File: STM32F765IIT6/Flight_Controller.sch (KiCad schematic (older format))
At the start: 1 part

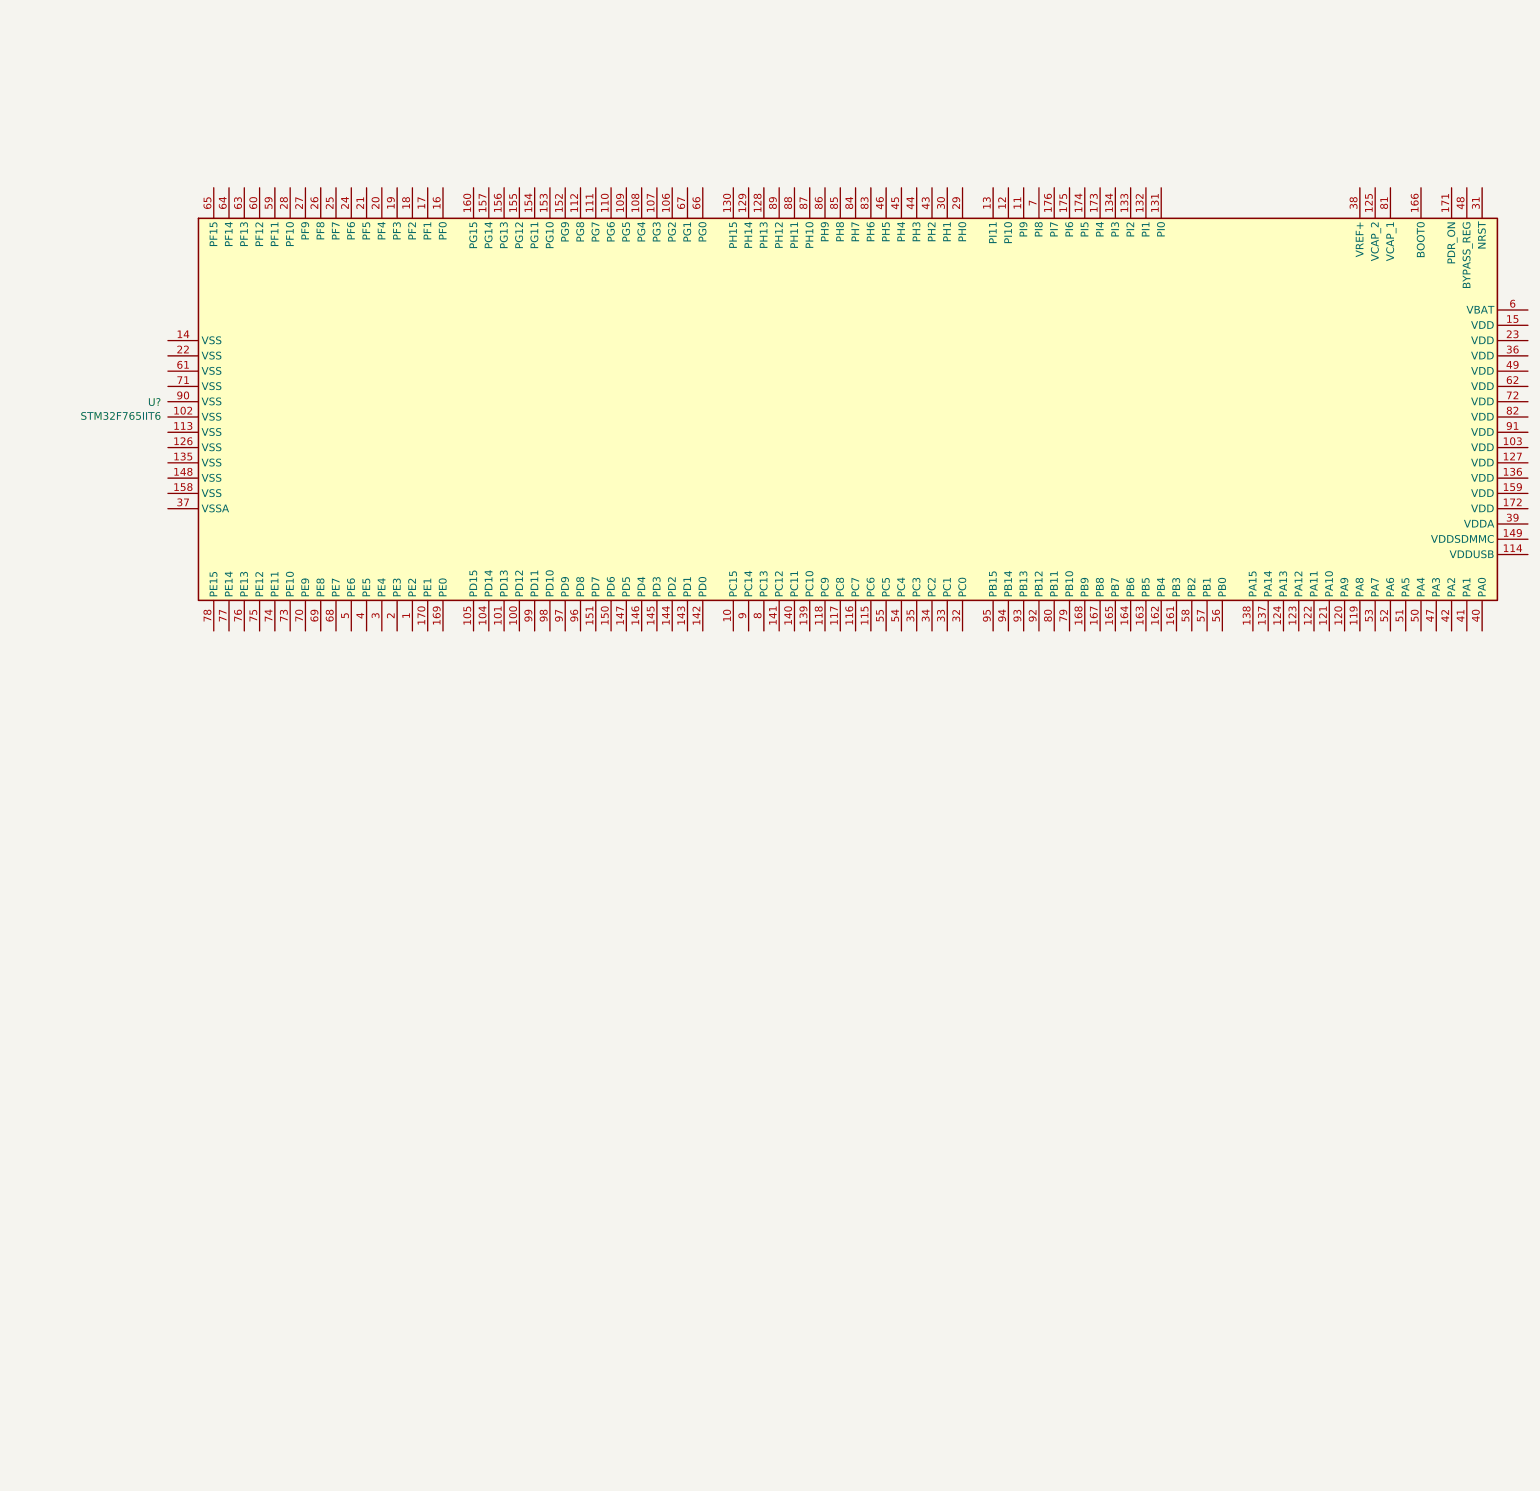
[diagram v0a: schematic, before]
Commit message: Update schematic to include all labels
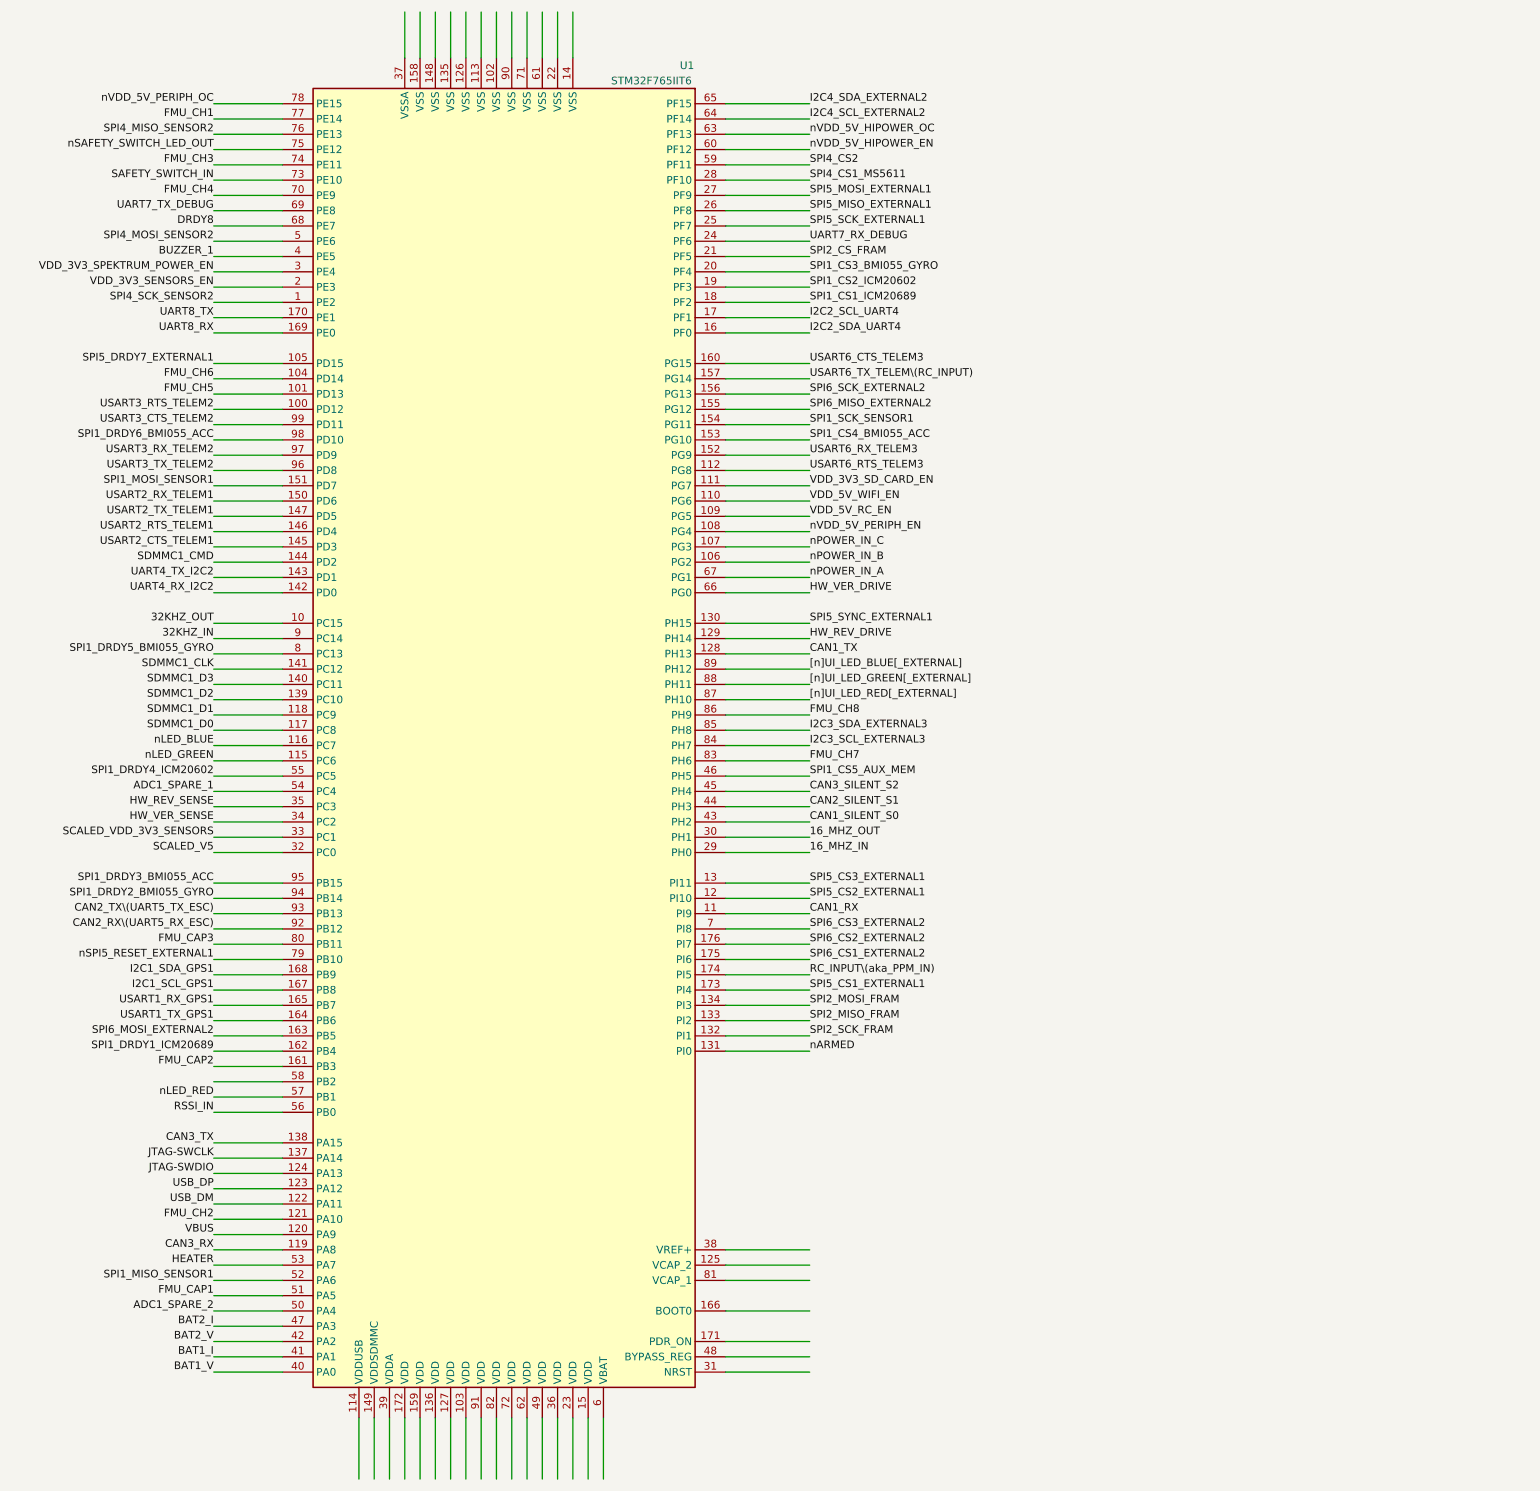
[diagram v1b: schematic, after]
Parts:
- gave numbers to parts that had none: 1
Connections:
- net labels added: 16_MHZ_IN, 16_MHZ_OUT, 32KHZ_IN, 32KHZ_OUT, ADC1_SPARE_1, ADC1_SPARE_2, BAT1_I, BAT1_V, BAT2_I, BAT2_V, BUZZER_1, CAN1_RX, CAN1_SILENT_S0, CAN1_TX, CAN2_RX\(UART5_RX_ESC), CAN2_SILENT_S1, CAN2_TX\(UART5_TX_ESC), CAN3_RX, CAN3_SILENT_S2, CAN3_TX, DRDY8, FMU_CAP1, FMU_CAP2, FMU_CAP3, FMU_CH1, FMU_CH2, FMU_CH3, FMU_CH4, FMU_CH5, FMU_CH6, FMU_CH7, FMU_CH8, HEATER, HW_REV_DRIVE, HW_REV_SENSE, HW_VER_DRIVE, HW_VER_SENSE, I2C1_SCL_GPS1, I2C1_SDA_GPS1, I2C2_SCL_UART4, I2C2_SDA_UART4, I2C3_SCL_EXTERNAL3, I2C3_SDA_EXTERNAL3, I2C4_SCL_EXTERNAL2, I2C4_SDA_EXTERNAL2, JTAG-SWCLK, JTAG-SWDIO, RC_INPUT\(aka_PPM_IN), RSSI_IN, SAFETY_SWITCH_IN, SCALED_V5, SCALED_VDD_3V3_SENSORS, SDMMC1_CLK, SDMMC1_CMD, SDMMC1_D0, SDMMC1_D1, SDMMC1_D2, SDMMC1_D3, SPI1_CS1_ICM20689, SPI1_CS2_ICM20602, SPI1_CS3_BMI055_GYRO, SPI1_CS4_BMI055_ACC, SPI1_CS5_AUX_MEM, SPI1_DRDY1_ICM20689, SPI1_DRDY2_BMI055_GYRO, SPI1_DRDY3_BMI055_ACC, SPI1_DRDY4_ICM20602, SPI1_DRDY5_BMI055_GYRO, SPI1_DRDY6_BMI055_ACC, SPI1_MISO_SENSOR1, SPI1_MOSI_SENSOR1, SPI1_SCK_SENSOR1, SPI2_CS_FRAM, SPI2_MISO_FRAM, SPI2_MOSI_FRAM, SPI2_SCK_FRAM, SPI4_CS1_MS5611, SPI4_CS2, SPI4_MISO_SENSOR2, SPI4_MOSI_SENSOR2, SPI4_SCK_SENSOR2, SPI5_CS1_EXTERNAL1, SPI5_CS2_EXTERNAL1, SPI5_CS3_EXTERNAL1, SPI5_DRDY7_EXTERNAL1, SPI5_MISO_EXTERNAL1, SPI5_MOSI_EXTERNAL1, SPI5_SCK_EXTERNAL1, SPI5_SYNC_EXTERNAL1, SPI6_CS1_EXTERNAL2, SPI6_CS2_EXTERNAL2, SPI6_CS3_EXTERNAL2, SPI6_MISO_EXTERNAL2, SPI6_MOSI_EXTERNAL2, SPI6_SCK_EXTERNAL2, UART4_RX_I2C2, UART4_TX_I2C2, UART7_RX_DEBUG, UART7_TX_DEBUG, UART8_RX, UART8_TX, USART1_RX_GPS1, USART1_TX_GPS1, USART2_CTS_TELEM1, USART2_RTS_TELEM1, USART2_RX_TELEM1, USART2_TX_TELEM1, USART3_CTS_TELEM2, USART3_RTS_TELEM2, USART3_RX_TELEM2, USART3_TX_TELEM2, USART6_CTS_TELEM3, USART6_RTS_TELEM3, USART6_RX_TELEM3, USART6_TX_TELEM\(RC_INPUT), USB_DM, USB_DP, VBUS, VDD_3V3_SD_CARD_EN, VDD_3V3_SENSORS_EN, VDD_3V3_SPEKTRUM_POWER_EN, VDD_5V_RC_EN, VDD_5V_WIFI_EN, [n]UI_LED_BLUE[_EXTERNAL], [n]UI_LED_GREEN[_EXTERNAL], [n]UI_LED_RED[_EXTERNAL], nARMED, nLED_BLUE, nLED_GREEN, nLED_RED, nPOWER_IN_A, nPOWER_IN_B, nPOWER_IN_C, nSAFETY_SWITCH_LED_OUT, nSPI5_RESET_EXTERNAL1, nVDD_5V_HIPOWER_EN, nVDD_5V_HIPOWER_OC, nVDD_5V_PERIPH_EN, nVDD_5V_PERIPH_OC
- wire segments 0 -> 176
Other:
- moved on the sheet: U1
